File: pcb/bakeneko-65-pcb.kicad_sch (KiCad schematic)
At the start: 19 parts, among them J1 JST SH 4-pin, J2 AVR-ISP-6, SW1 Reset, U1 SRV05-4, U2 ATmega32U4-AU, U3 ATmega32U4-M, Y1 16MHz

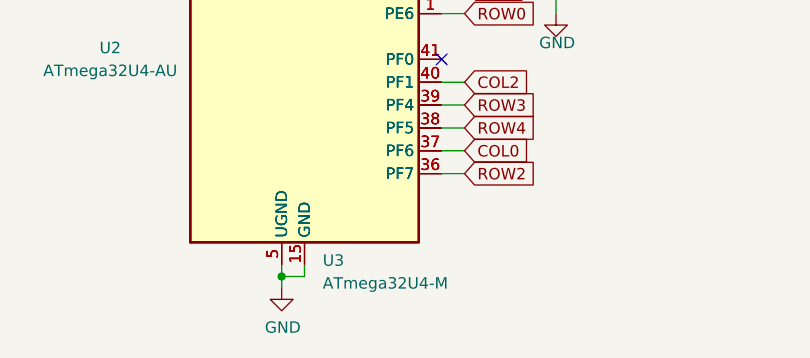
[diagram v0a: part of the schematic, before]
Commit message: Small updates - USB routing
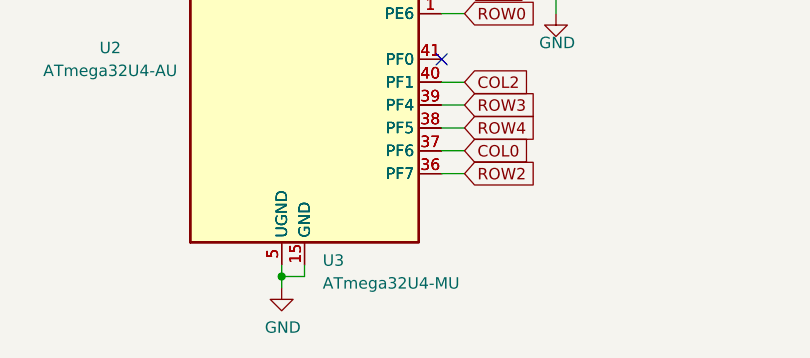
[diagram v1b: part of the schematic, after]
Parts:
- U3: value ATmega32U4-M -> ATmega32U4-MU; LCSC (none) -> C112161
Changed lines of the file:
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@@
       (effects (font (size 1.27 1.27)) (justify left))
     )
-    (property "Value" "ATmega32U4-M" (id 1) (at 60.4394 176.0173 0)
+    (property "Value" "ATmega32U4-MU" (id 1) (at 60.4394 176.0173 0)
       (effects (font (size 1.27 1.27)) (justify left))
     )
@@
     )
     (property "Datasheet" "http://ww1.microchip.com/downloads/en/DeviceDoc/Atmel-7766-8-bit-AVR-ATmega16U4-32U4_Datasheet.pdf" (id 3) (at 58.42 128.27 0)
+      (effects (font (size 1.27 1.27)) hide)
+    )
+    (property "LCSC" "C112161" (id 4) (at 58.42 128.27 0)
       (effects (font (size 1.27 1.27)) hide)
     )
@@
     )
     (path "/d293ffd0-0d39-4336-b48b-d86bab8e7171"
-      (reference "U3") (unit 1) (value "ATmega32U4-M") (footprint "Package_DFN_QFN:QFN-44-1EP_7x7mm_P0.5mm_EP5.2x5.2mm")
+      (reference "U3") (unit 1) (value "ATmega32U4-MU") (footprint "Package_DFN_QFN:QFN-44-1EP_7x7mm_P0.5mm_EP5.2x5.2mm")
     )
     (path "/00000000-0000-0000-0000-00005f293f4e"

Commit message: Revert "Small updates - USB routing"
This reverts commit 01b81f097f4a432426e23b6d52fb9b838f85ddba.
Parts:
- U3: value ATmega32U4-MU -> ATmega32U4-M; LCSC C112161 -> (none)
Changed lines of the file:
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@@
       (effects (font (size 1.27 1.27)) (justify left))
     )
-    (property "Value" "ATmega32U4-MU" (id 1) (at 60.4394 176.0173 0)
+    (property "Value" "ATmega32U4-M" (id 1) (at 60.4394 176.0173 0)
       (effects (font (size 1.27 1.27)) (justify left))
     )
@@
     )
     (property "Datasheet" "http://ww1.microchip.com/downloads/en/DeviceDoc/Atmel-7766-8-bit-AVR-ATmega16U4-32U4_Datasheet.pdf" (id 3) (at 58.42 128.27 0)
-      (effects (font (size 1.27 1.27)) hide)
-    )
-    (property "LCSC" "C112161" (id 4) (at 58.42 128.27 0)
       (effects (font (size 1.27 1.27)) hide)
     )
@@
     )
     (path "/d293ffd0-0d39-4336-b48b-d86bab8e7171"
-      (reference "U3") (unit 1) (value "ATmega32U4-MU") (footprint "Package_DFN_QFN:QFN-44-1EP_7x7mm_P0.5mm_EP5.2x5.2mm")
+      (reference "U3") (unit 1) (value "ATmega32U4-M") (footprint "Package_DFN_QFN:QFN-44-1EP_7x7mm_P0.5mm_EP5.2x5.2mm")
     )
     (path "/00000000-0000-0000-0000-00005f293f4e"

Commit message: Revert "Dual MCU footprint update"
This reverts commit d3ec1e4d8a5bc08a1e6c0b7459cdd594f23042e6.
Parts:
- removed U3: ATmega32U4-M, Package_DFN_QFN:QFN-44-1EP_7x7mm_P0.5mm_EP5.2x5.2mm, symbol MCU_Microchip_ATmega:ATmega32U4-M
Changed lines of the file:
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@@
     (pin "1")
-  )
-  (symbol (lib_id "MCU_Microchip_ATmega:ATmega32U4-M") (at 58.42 128.27 0) (unit 1)
-    (in_bom yes) (on_board yes) (fields_autoplaced)
-    (property "Reference" "U3" (id 0) (at 60.4394 173.4804 0)
-      (effects (font (size 1.27 1.27)) (justify left))
-    )
-    (property "Value" "ATmega32U4-M" (id 1) (at 60.4394 176.0173 0)
-      (effects (font (size 1.27 1.27)) (justify left))
-    )
-    (property "Footprint" "Package_DFN_QFN:QFN-44-1EP_7x7mm_P0.5mm_EP5.2x5.2mm" (id 2) (at 58.42 128.27 0)
-      (effects (font (size 1.27 1.27) italic) hide)
-    )
-    (property "Datasheet" "http://ww1.microchip.com/downloads/en/DeviceDoc/Atmel-7766-8-bit-AVR-ATmega16U4-32U4_Datasheet.pdf" (id 3) (at 58.42 128.27 0)
-      (effects (font (size 1.27 1.27)) hide)
-    )
-    (pin "1")
-    (pin "10")
-    (pin "11")
-    (pin "12")
-    (pin "13")
-    (pin "14")
-    (pin "15")
-    (pin "16")
-    (pin "17")
-    (pin "18")
-    (pin "19")
-    (pin "2")
-    (pin "20")
-    (pin "21")
-    (pin "22")
-    (pin "23")
-    (pin "24")
-    (pin "25")
-    (pin "26")
-    (pin "27")
-    (pin "28")
-    (pin "29")
-    (pin "3")
-    (pin "30")
-    (pin "31")
-    (pin "32")
-    (pin "33")
-    (pin "34")
-    (pin "35")
-    (pin "36")
-    (pin "37")
-    (pin "38")
-    (pin "39")
-    (pin "4")
-    (pin "40")
-    (pin "41")
-    (pin "42")
-    (pin "43")
-    (pin "44")
-    (pin "45")
-    (pin "5")
-    (pin "6")
-    (pin "7")
-    (pin "8")
-    (pin "9")
   )
   (sheet (at 185.42 87.63) (size 45.72 53.34) (fields_autoplaced)
@@
       (reference "U2") (unit 1) (value "ATmega32U4-AU") (footprint "Package_QFP:TQFP-44_10x10mm_P0.8mm")
     )
-    (path "/d293ffd0-0d39-4336-b48b-d86bab8e7171"
-      (reference "U3") (unit 1) (value "ATmega32U4-M") (footprint "Package_DFN_QFN:QFN-44-1EP_7x7mm_P0.5mm_EP5.2x5.2mm")
-    )
     (path "/00000000-0000-0000-0000-00005f293f4e"

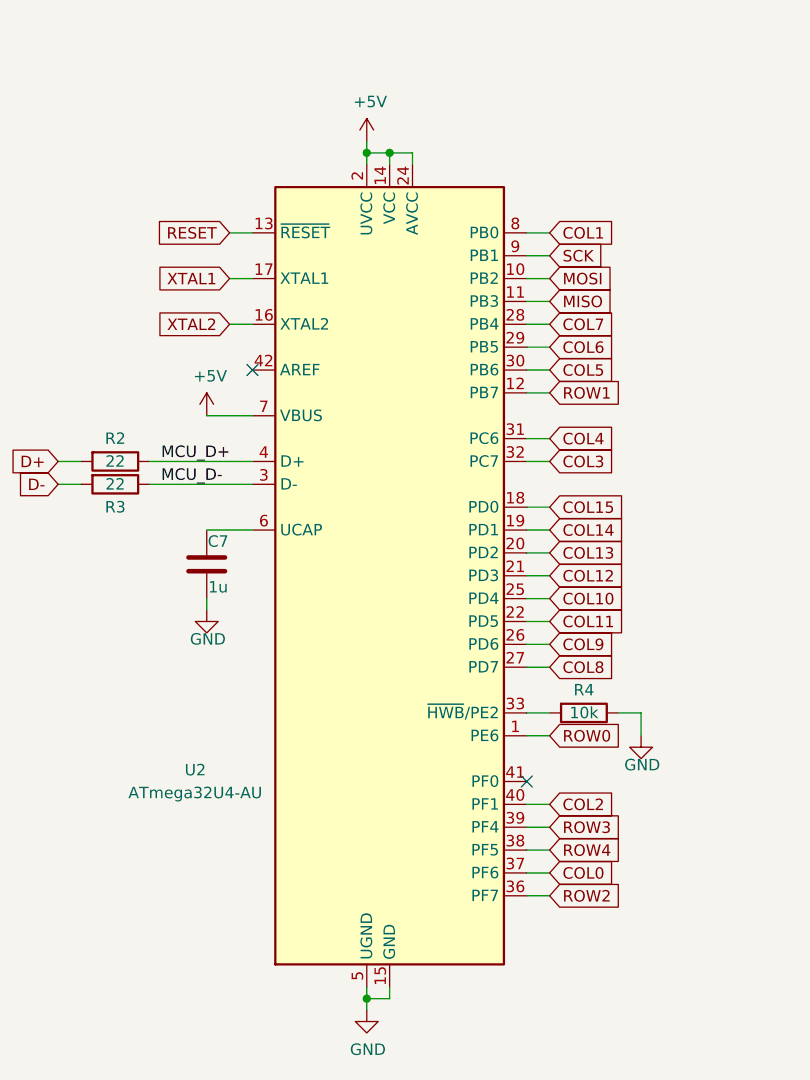
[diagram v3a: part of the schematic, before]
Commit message: Dual MCU footprint update
Ability to use either ATMega32U4 footprint - AU or MU.
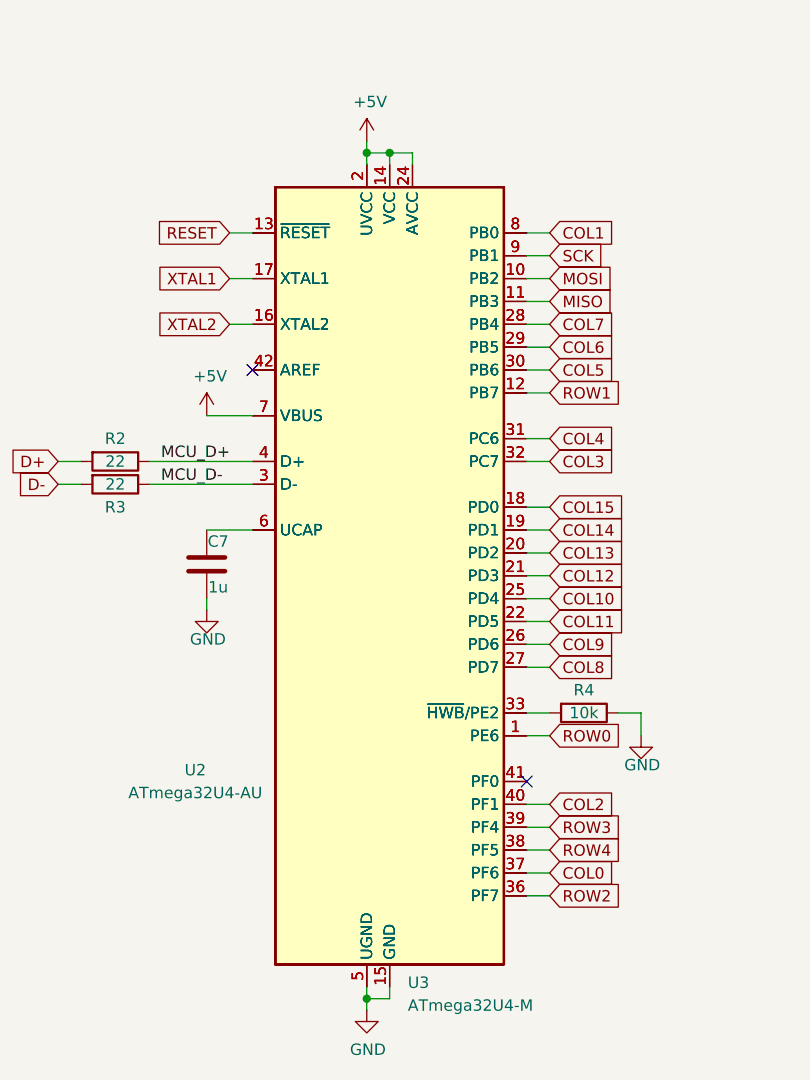
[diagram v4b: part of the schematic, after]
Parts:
- added U3: ATmega32U4-M, Package_DFN_QFN:QFN-44-1EP_7x7mm_P0.5mm_EP5.2x5.2mm, symbol MCU_Microchip_ATmega:ATmega32U4-M
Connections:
- net +5V: now also U3.14 (VCC), U3.2 (UVCC), U3.24 (AVCC), U3.34 (VCC), U3.44 (AVCC), U3.7 (VBUS)
- net COL0: now also U3.37 (PF6)
- net COL1: now also U3.8 (PB0)
- net COL10: now also U3.25 (PD4)
- net COL11: now also U3.22 (PD5)
- net COL12: now also U3.21 (PD3)
- net COL13: now also U3.20 (PD2)
- net COL14: now also U3.19 (PD1)
- net COL15: now also U3.18 (PD0)
- net COL2: now also U3.40 (PF1)
- net COL3: now also U3.32 (PC7)
- net COL4: now also U3.31 (PC6)
- net COL5: now also U3.30 (PB6)
- net COL6: now also U3.29 (PB5)
- net COL7: now also U3.28 (PB4)
- net COL8: now also U3.27 (PD7)
- net COL9: now also U3.26 (PD6)
- net GND: now also U3.15 (GND), U3.23 (GND), U3.35 (GND), U3.43 (GND), U3.45 (GND), U3.5 (UGND)
- net MCU_D+: now also U3.4 (D+)
- net MCU_D-: now also U3.3 (D-)
- net MISO: now also U3.11 (PB3)
- net MOSI: now also U3.10 (PB2)
- net RESET: now also U3.13 (~{RESET})
- net ROW0: now also U3.1 (PE6)
- net ROW1: now also U3.12 (PB7)
- net ROW2: now also U3.36 (PF7)
- net ROW3: now also U3.39 (PF4)
- net ROW4: now also U3.38 (PF5)
- net SCK: now also U3.9 (PB1)
- net XTAL1: now also U3.17 (XTAL1)
- net XTAL2: now also U3.16 (XTAL2)
- net at R4.2, U2.33 (~{HWB}/PE2): now also U3.33 (~{HWB}/PE2)
- net at U2.41 (PF0): now also U3.41 (PF0)
- net at U2.42 (AREF): now also U3.42 (AREF)
- net at C7.1, U2.6 (UCAP): now also U3.6 (UCAP)
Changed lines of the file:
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@@
     (pin "1")
+  )
+  (symbol (lib_id "MCU_Microchip_ATmega:ATmega32U4-M") (at 58.42 128.27 0) (unit 1)
+    (in_bom yes) (on_board yes) (fields_autoplaced)
+    (property "Reference" "U3" (id 0) (at 60.4394 173.4804 0)
+      (effects (font (size 1.27 1.27)) (justify left))
+    )
+    (property "Value" "ATmega32U4-M" (id 1) (at 60.4394 176.0173 0)
+      (effects (font (size 1.27 1.27)) (justify left))
+    )
+    (property "Footprint" "Package_DFN_QFN:QFN-44-1EP_7x7mm_P0.5mm_EP5.2x5.2mm" (id 2) (at 58.42 128.27 0)
+      (effects (font (size 1.27 1.27) italic) hide)
+    )
+    (property "Datasheet" "http://ww1.microchip.com/downloads/en/DeviceDoc/Atmel-7766-8-bit-AVR-ATmega16U4-32U4_Datasheet.pdf" (id 3) (at 58.42 128.27 0)
+      (effects (font (size 1.27 1.27)) hide)
+    )
+    (pin "1")
+    (pin "10")
+    (pin "11")
+    (pin "12")
+    (pin "13")
+    (pin "14")
+    (pin "15")
+    (pin "16")
+    (pin "17")
+    (pin "18")
+    (pin "19")
+    (pin "2")
+    (pin "20")
+    (pin "21")
+    (pin "22")
+    (pin "23")
+    (pin "24")
+    (pin "25")
+    (pin "26")
+    (pin "27")
+    (pin "28")
+    (pin "29")
+    (pin "3")
+    (pin "30")
+    (pin "31")
+    (pin "32")
+    (pin "33")
+    (pin "34")
+    (pin "35")
+    (pin "36")
+    (pin "37")
+    (pin "38")
+    (pin "39")
+    (pin "4")
+    (pin "40")
+    (pin "41")
+    (pin "42")
+    (pin "43")
+    (pin "44")
+    (pin "45")
+    (pin "5")
+    (pin "6")
+    (pin "7")
+    (pin "8")
+    (pin "9")
   )
   (sheet (at 185.42 87.63) (size 45.72 53.34) (fields_autoplaced)
@@
       (reference "U2") (unit 1) (value "ATmega32U4-AU") (footprint "Package_QFP:TQFP-44_10x10mm_P0.8mm")
     )
+    (path "/d293ffd0-0d39-4336-b48b-d86bab8e7171"
+      (reference "U3") (unit 1) (value "ATmega32U4-M") (footprint "Package_DFN_QFN:QFN-44-1EP_7x7mm_P0.5mm_EP5.2x5.2mm")
+    )
     (path "/00000000-0000-0000-0000-00005f293f4e"
